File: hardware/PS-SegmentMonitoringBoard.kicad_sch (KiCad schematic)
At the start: 2 parts

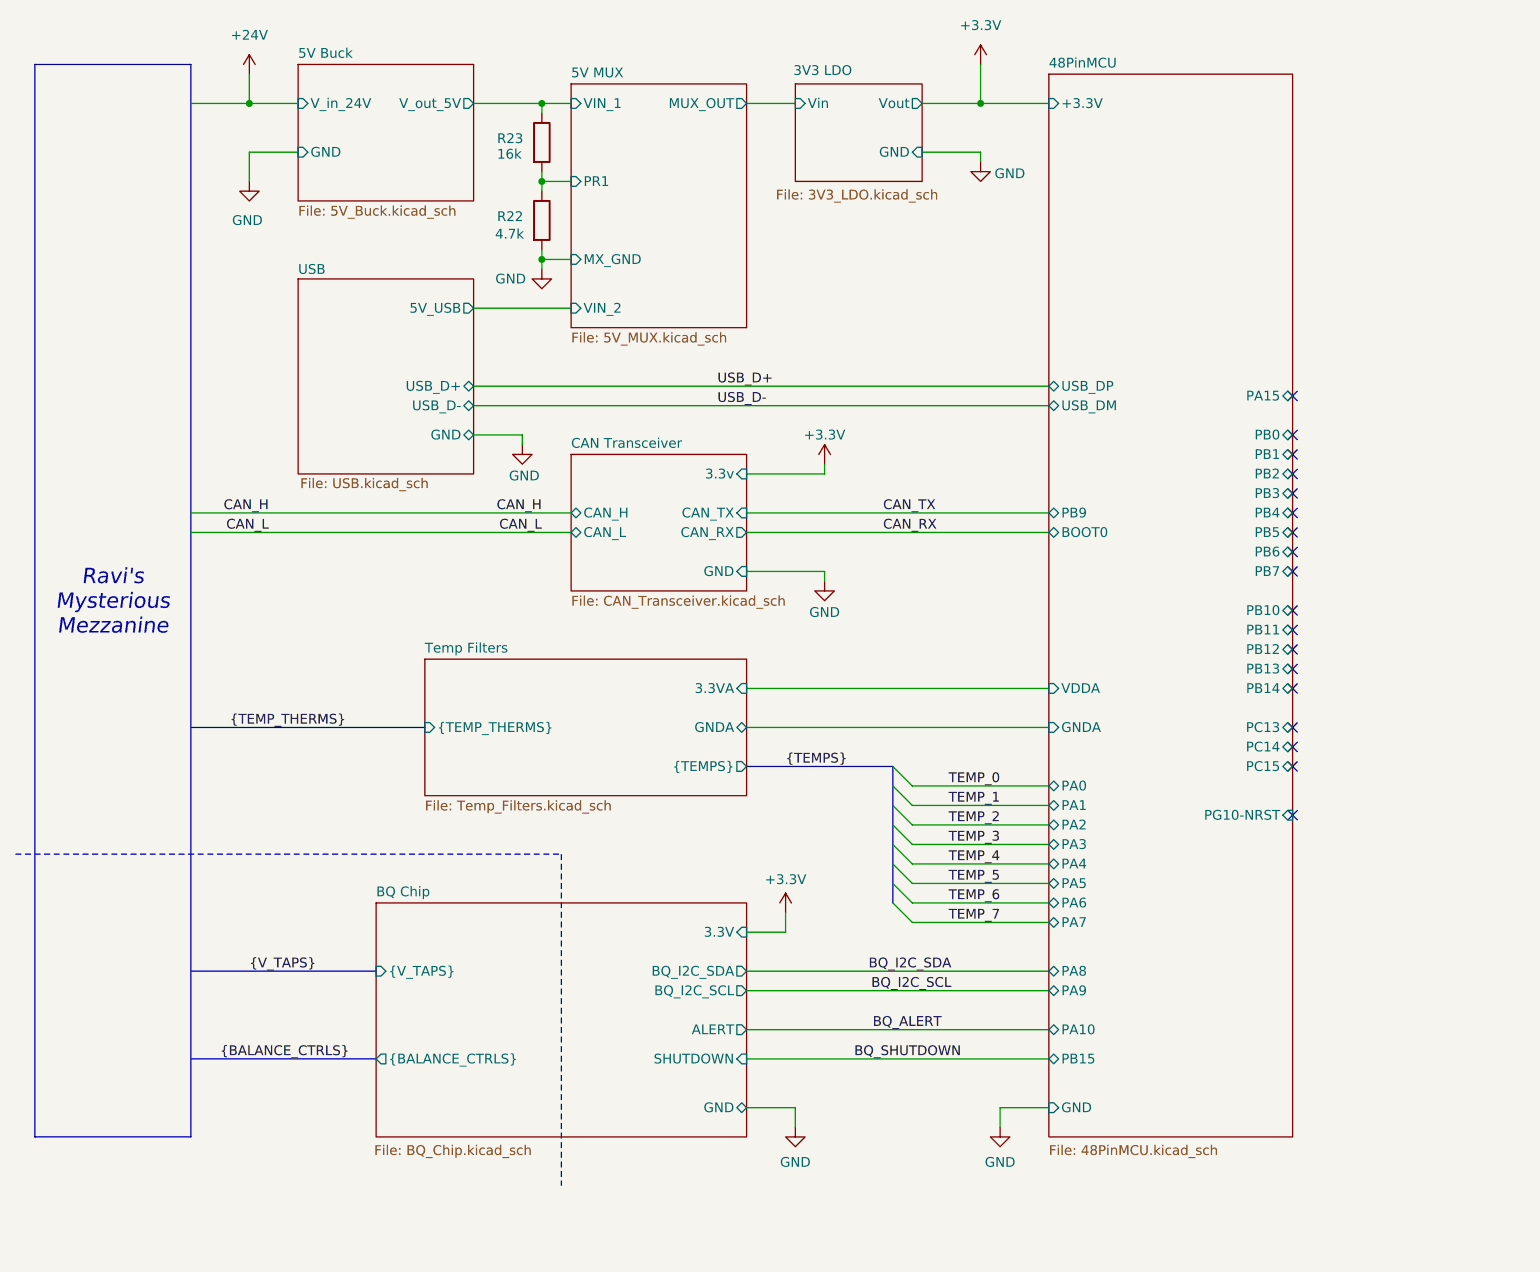
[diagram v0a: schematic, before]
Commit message: New BMS arch and IC
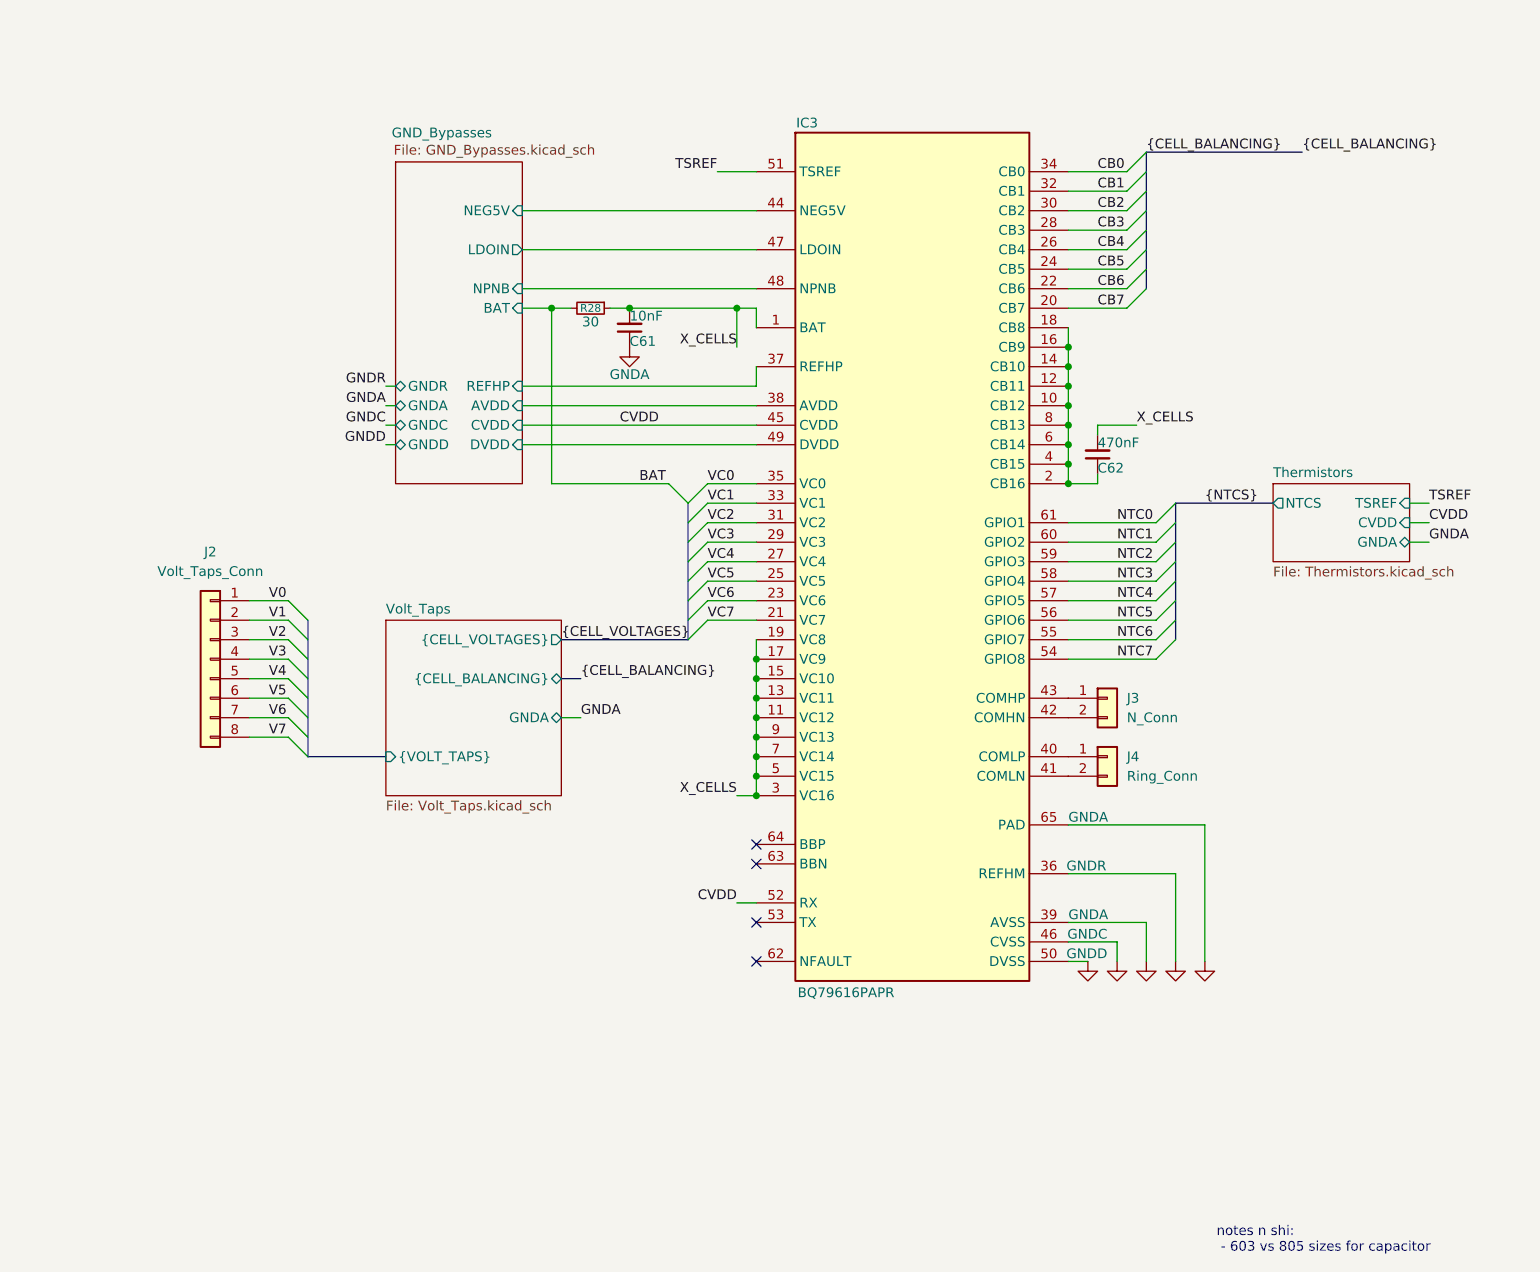
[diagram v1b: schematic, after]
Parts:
- removed R22: 4.7k, symbol Device:R
- removed R23: 16k, symbol Device:R
- added C61: 10nF, symbol Device:C_Small
- added C62: 470nF, symbol Device:C_Small
- added IC3: BQ79616PAPR, QFP50P1200X1200X120-65N, symbol custom_symbols:BQ79616PAPR
- added J2: Volt_Taps_Conn, symbol Connector_Generic:Conn_01x08
- added J3: N_Conn, symbol Connector_Generic:Conn_01x02
- added J4: Ring_Conn, symbol Connector_Generic:Conn_01x02
- added R28: 30, symbol Device:R_Small
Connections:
- new net: IC3.43 (COMHP), J3.1 (Pin_1)
- new net: IC3.42 (COMHN), J3.2 (Pin_2)
- new net: C62.1, IC3.10 (CB12), IC3.12 (CB11), IC3.14 (CB10), IC3.16 (CB9), IC3.18 (CB8), IC3.2 (CB16), IC3.4 (CB15), IC3.6 (CB14), IC3.8 (CB13)
- new net: IC3.40 (COMLP), J4.1 (Pin_1)
- new net: IC3.41 (COMLN), J4.2 (Pin_2)
- new net BAT: R28.2
- new net CB0: IC3.34 (CB0)
- new net CB1: IC3.32 (CB1)
- new net CB2: IC3.30 (CB2)
- new net CB3: IC3.28 (CB3)
- new net CB4: IC3.26 (CB4)
- new net CB5: IC3.24 (CB5)
- new net CB6: IC3.22 (CB6)
- new net CB7: IC3.20 (CB7)
- new net CVDD: IC3.45 (CVDD), IC3.52 (RX)
- new net GNDA: C61.1, IC3.39 (AVSS), IC3.65 (PAD)
- new net GNDC: IC3.46 (CVSS)
- new net GNDD: IC3.50 (DVSS)
- new net GNDR: IC3.36 (REFHM)
- new net GND_Bypasses/AVDD: IC3.38 (AVDD)
- new net GND_Bypasses/DVDD: IC3.49 (DVDD)
- new net GND_Bypasses/LDOIN: IC3.47 (LDOIN)
- new net GND_Bypasses/NEG5V: IC3.44 (NEG5V)
- new net GND_Bypasses/NPNB: IC3.48 (NPNB)
- new net GND_Bypasses/REFHP: IC3.37 (REFHP)
- new net NTC0: IC3.61 (GPIO1)
- new net NTC1: IC3.60 (GPIO2)
- new net NTC2: IC3.59 (GPIO3)
- new net NTC3: IC3.58 (GPIO4)
- new net NTC4: IC3.57 (GPIO5)
- new net NTC5: IC3.56 (GPIO6)
- new net NTC6: IC3.55 (GPIO7)
- new net NTC7: IC3.54 (GPIO8)
- new net TSREF: IC3.51 (TSREF)
- new net V0: J2.1 (Pin_1)
- new net V1: J2.2 (Pin_2)
- new net V2: J2.3 (Pin_3)
- new net V3: J2.4 (Pin_4)
- new net V4: J2.5 (Pin_5)
- new net V5: J2.6 (Pin_6)
- new net V6: J2.7 (Pin_7)
- new net V7: J2.8 (Pin_8)
- new net VC0: IC3.35 (VC0)
- new net VC1: IC3.33 (VC1)
- new net VC2: IC3.31 (VC2)
- new net VC3: IC3.29 (VC3)
- new net VC4: IC3.27 (VC4)
- new net VC5: IC3.25 (VC5)
- new net VC6: IC3.23 (VC6)
- new net VC7: IC3.21 (VC7)
- new net X_CELLS: C61.2, C62.2, IC3.1 (BAT), IC3.11 (VC12), IC3.13 (VC11), IC3.15 (VC10), IC3.17 (VC9), IC3.19 (VC8), IC3.3 (VC16), IC3.5 (VC15), IC3.7 (VC14), IC3.9 (VC13), R28.1
- no-connect marks 18 -> 4
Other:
- removed sheet 3V3 LDO
- removed sheet 48PinMCU
- removed sheet 5V Buck
- removed sheet 5V MUX
- removed sheet BQ Chip
- removed sheet CAN Transceiver
- removed sheet Temp Filters
- removed sheet USB
- added sheet GND_Bypasses (GND_Bypasses.kicad_sch)
- added sheet Thermistors (Thermistors.kicad_sch)
- added sheet Volt_Taps (Volt_Taps.kicad_sch)
- note added: "notes n shi: - 603 vs 805 sizes for capacitor"
- note removed: "Ravi's Mysterious Mezzanine"
